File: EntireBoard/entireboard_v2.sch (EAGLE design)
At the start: 47 parts, among them J1 FTSH-105-01-XXX-DV-K, P1 0532610271, U1 YKA, U2 RHD2216_QFN

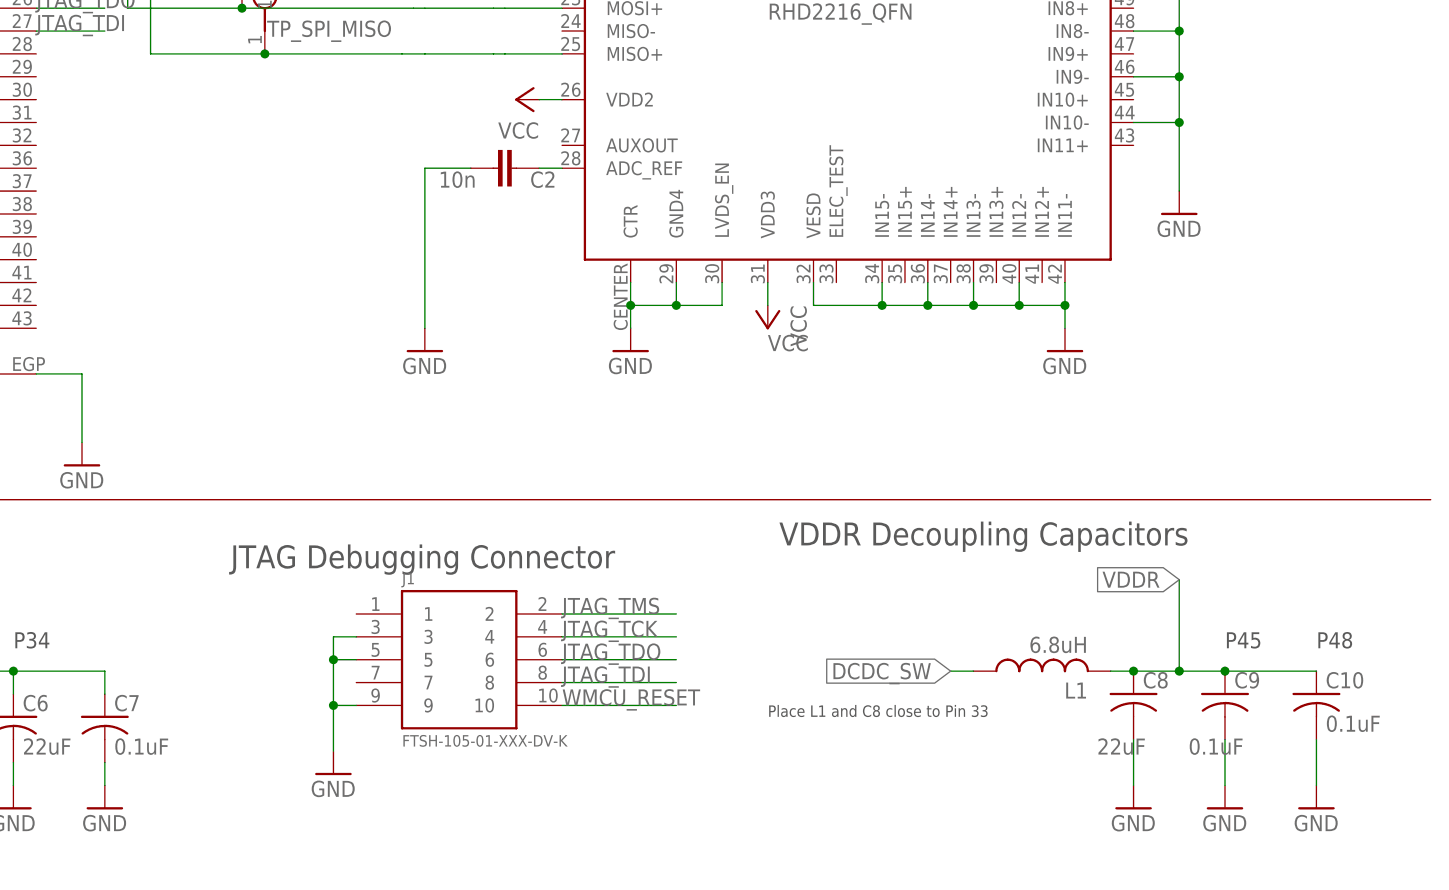
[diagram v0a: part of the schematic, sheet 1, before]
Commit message: 2 layer 6x6 cm board
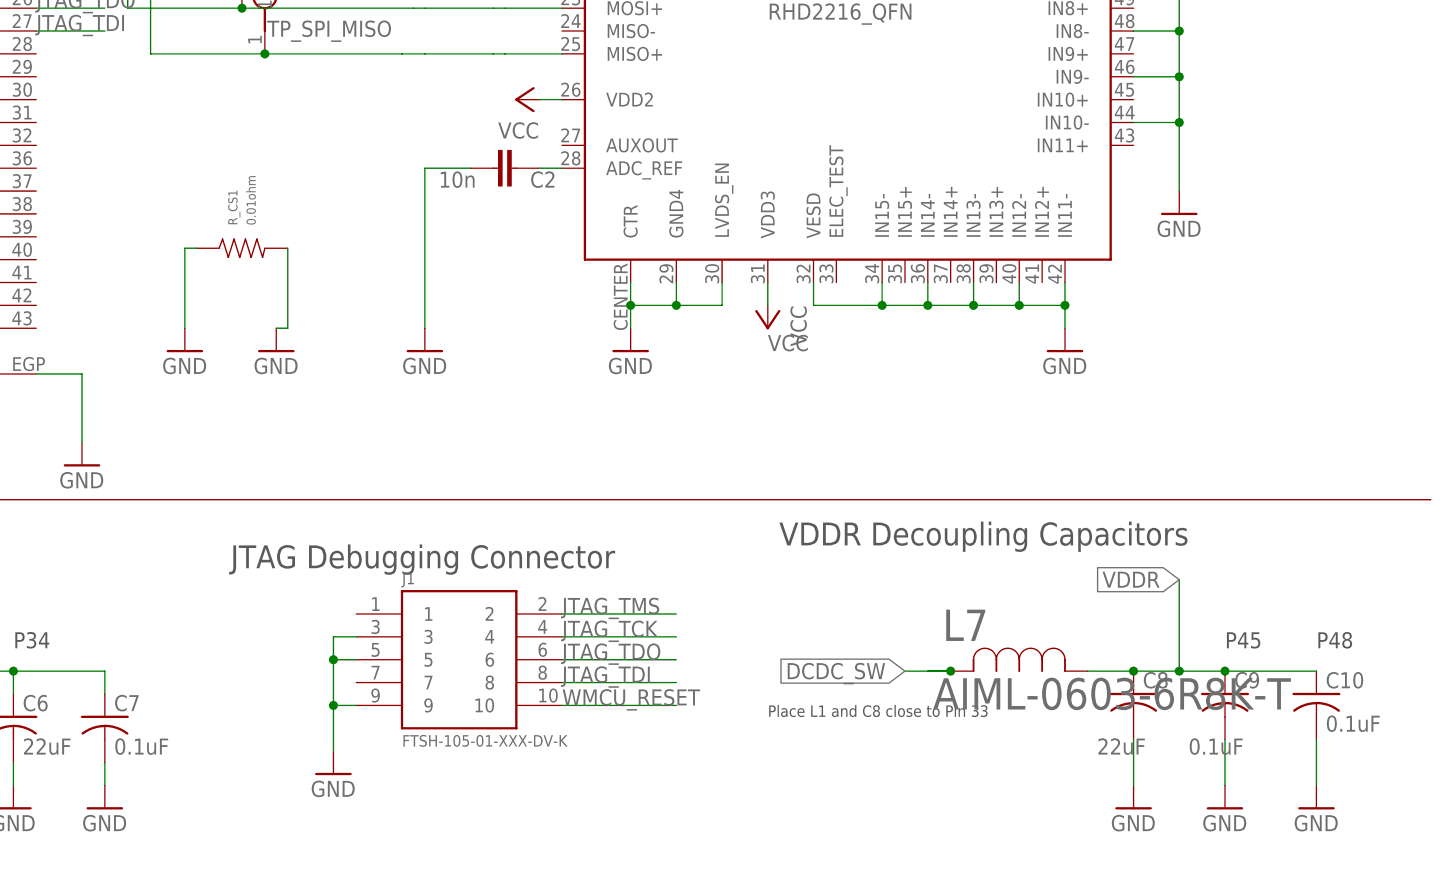
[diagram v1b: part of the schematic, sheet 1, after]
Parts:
- removed L6: 2.4nH, AxonMobile:L-SMD
- added L7: AIML-0603-6R8K-T, inductor_0603:AIML-0603-6R8K-T
- added R_CS1: 0.01ohm, MF_Passives:RESISTOR_0402
- L1: value 6.8uH -> 2.4nH; device AxonMobile:L-SMD -> rcl-2:L-USL0201
- L3: device AxonMobile:L-SMD -> rcl-2:L-USL0201
- L4: value 2nH -> 2.4nH; device AxonMobile:L-SMD -> rcl-2:L-USL0201
- L5: value 2.4nH -> 2nH; device AxonMobile:L-SMD -> rcl-2:L-USL0201
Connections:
- net DCDC_SW: now also L7.2; no longer L1.1
- net GND: now also R_CS1.P$1, R_CS1.P$2
- net N$12: now also L1.2; no longer L6.2
- net N$7: now also L5.2; no longer L3.2
- net N$8: now also L3.2, L5.1; no longer L3.1, L4.2
- net N$9: now also L3.1, L4.2; no longer L4.1, L5.2
- net RF_N: now also L4.1; no longer L5.1
- net RF_P: now also L1.1; no longer L6.1
- net VDDR: now also L7.1; no longer L1.2
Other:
- moved on the sheet: L3, L4, L5
